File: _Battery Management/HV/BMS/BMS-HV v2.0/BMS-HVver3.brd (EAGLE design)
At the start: 152.4 x 124.8 mm, 423 parts, among them J3 M2S02B-PASK-2(LF)(SN), J4 M2S02B-PASK-2(LF)(SN), Q1 BSS308PE, Q10 BSS308PE, Q11 BSS308PE, Q12 BSS308PE, Q13 BSS308PE, Q14 BSS308PE, Q15 BSS308PE, Q16 BSS308PE, Q17 BSS308PE, Q18 BSS308PE, Q19 BSS308PE, Q2 BSS308PE, Q20 BSS308PE, Q21 BSS308PE, Q22 BSS308PE, Q23 BSS308PE, Q24 BSS308PE, Q25 BSS308PE, Q26 BSS308PE, Q27 BSS308PE, Q28 BSS308PE, Q29 BSS308PE, Q3 BSS308PE, Q30 BSS308PE, Q31 BSS308PE, Q32 BSS308PE, Q33 BSS308PE, Q34 BSS308PE, Q35 BSS308PE, Q36 BSS308PE, Q37 BSS308PE, Q38 BSS308PE, Q39 BSS308PE, Q4 BSS308PE, Q5 BSS308PE, Q6 BSS308PE, Q7 BSS308PE, Q8 BSS308PE, Q9 BSS308PE, U1 LTC6804-2, U2 LTC6804-2, U3 LTC6804-2

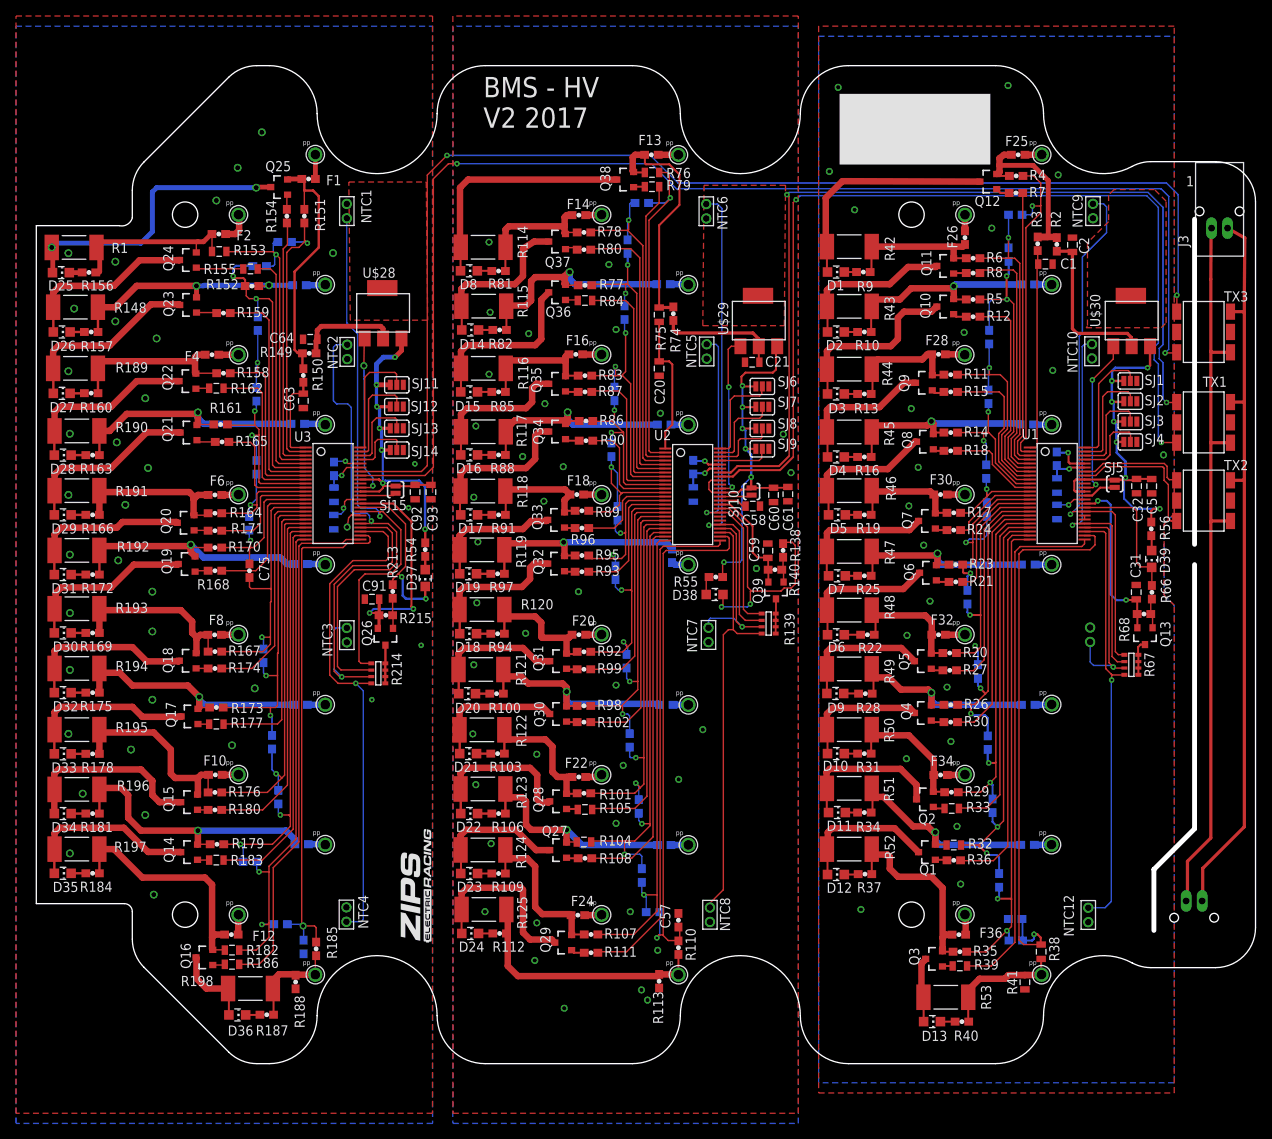
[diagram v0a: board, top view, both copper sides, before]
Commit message: 
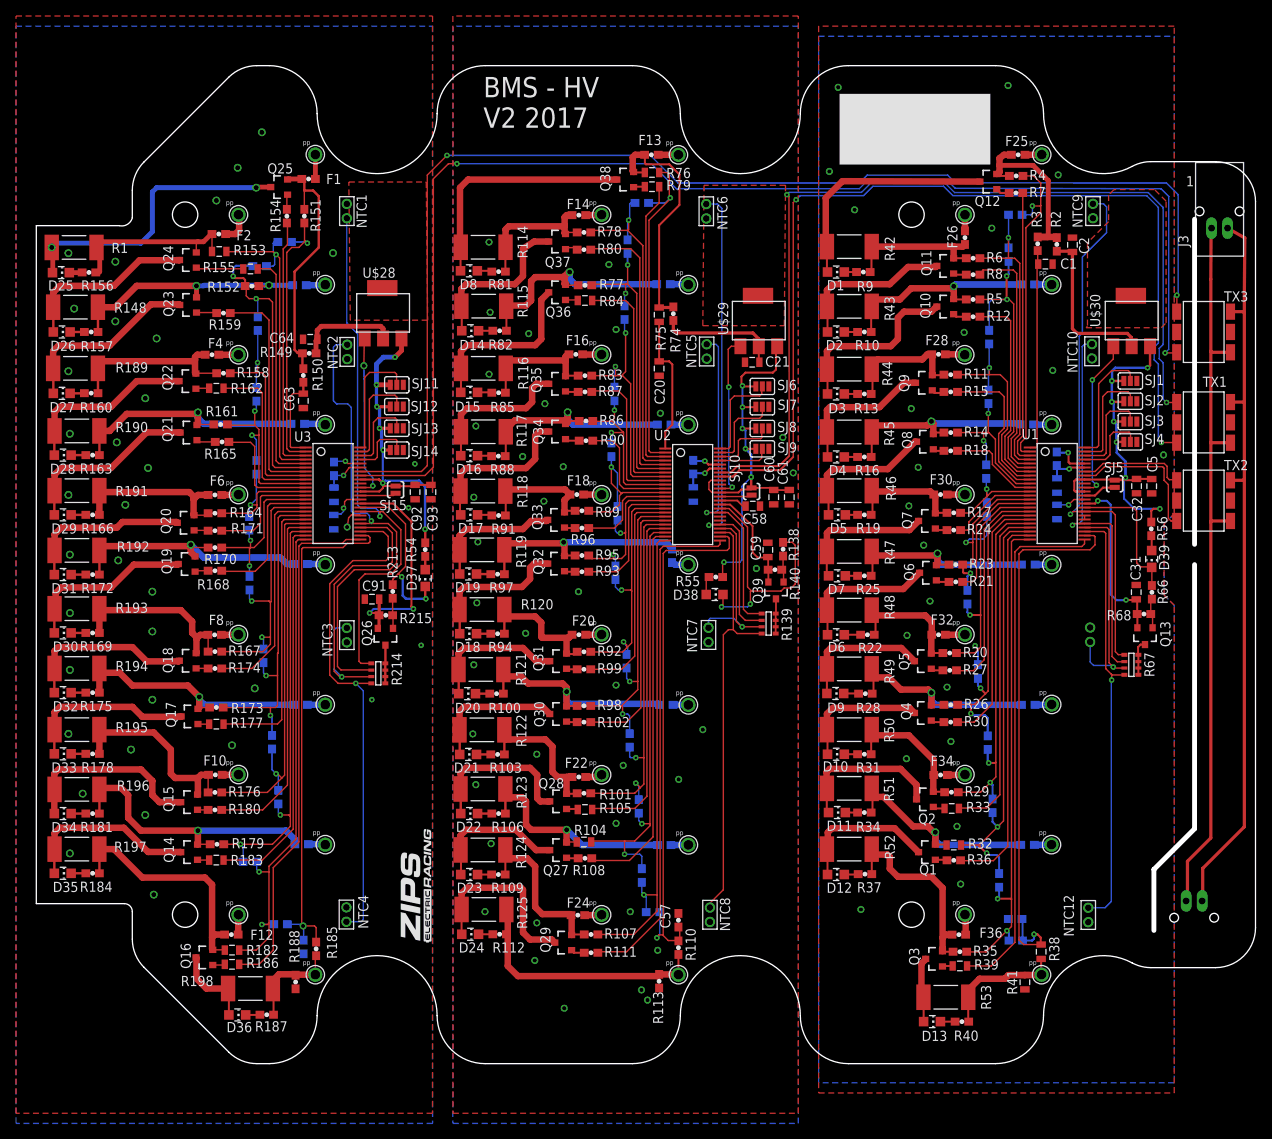
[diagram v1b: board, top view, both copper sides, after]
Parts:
- moved C75 1.55 mm to (-49.6, -2.31), flipped to the bottom
- moved C61 0.42 mm to (17.9, 8.43)
- moved C60 0.28 mm to (16.0, 8.43)
- moved R8 0.20 mm to (40.9, 36.2)
- moved R88 0.15 mm to (-18.4, 13.6)
- moved R138 0.15 mm to (17.1, 1.93)
- moved R109 0.13 mm to (-18.4, -38.7)
- moved D23 0.13 mm to (-22.1, -38.7)
- moved D14 0.10 mm to (-22.0, 29.2)
- moved D21 0.10 mm to (-22.2, -23.7)
- moved R103 0.10 mm to (-18.5, -23.7)
- moved R82 0.10 mm to (-18.3, 29.2)
- moved R85 0.10 mm to (-18.4, 21.5)
- moved C59 0.10 mm to (15.2, 1.84)
- moved D16 0.10 mm to (-22.1, 13.6)
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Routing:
- net C30: track 19.9 -> 21.5 mm, vias 1 -> 2
- net IMA: track 120.5 -> 121.5 mm
- net IPA: track 116.4 -> 117.4 mm
- net IMA2: track 161.4 -> 162.4 mm
- net IPA2: track 156.6 -> 157.4 mm
- net VREG: track 57.8 -> 57.3 mm
- net C31: track 34.3 -> 34.2 mm, vias 1 -> 2

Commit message: 
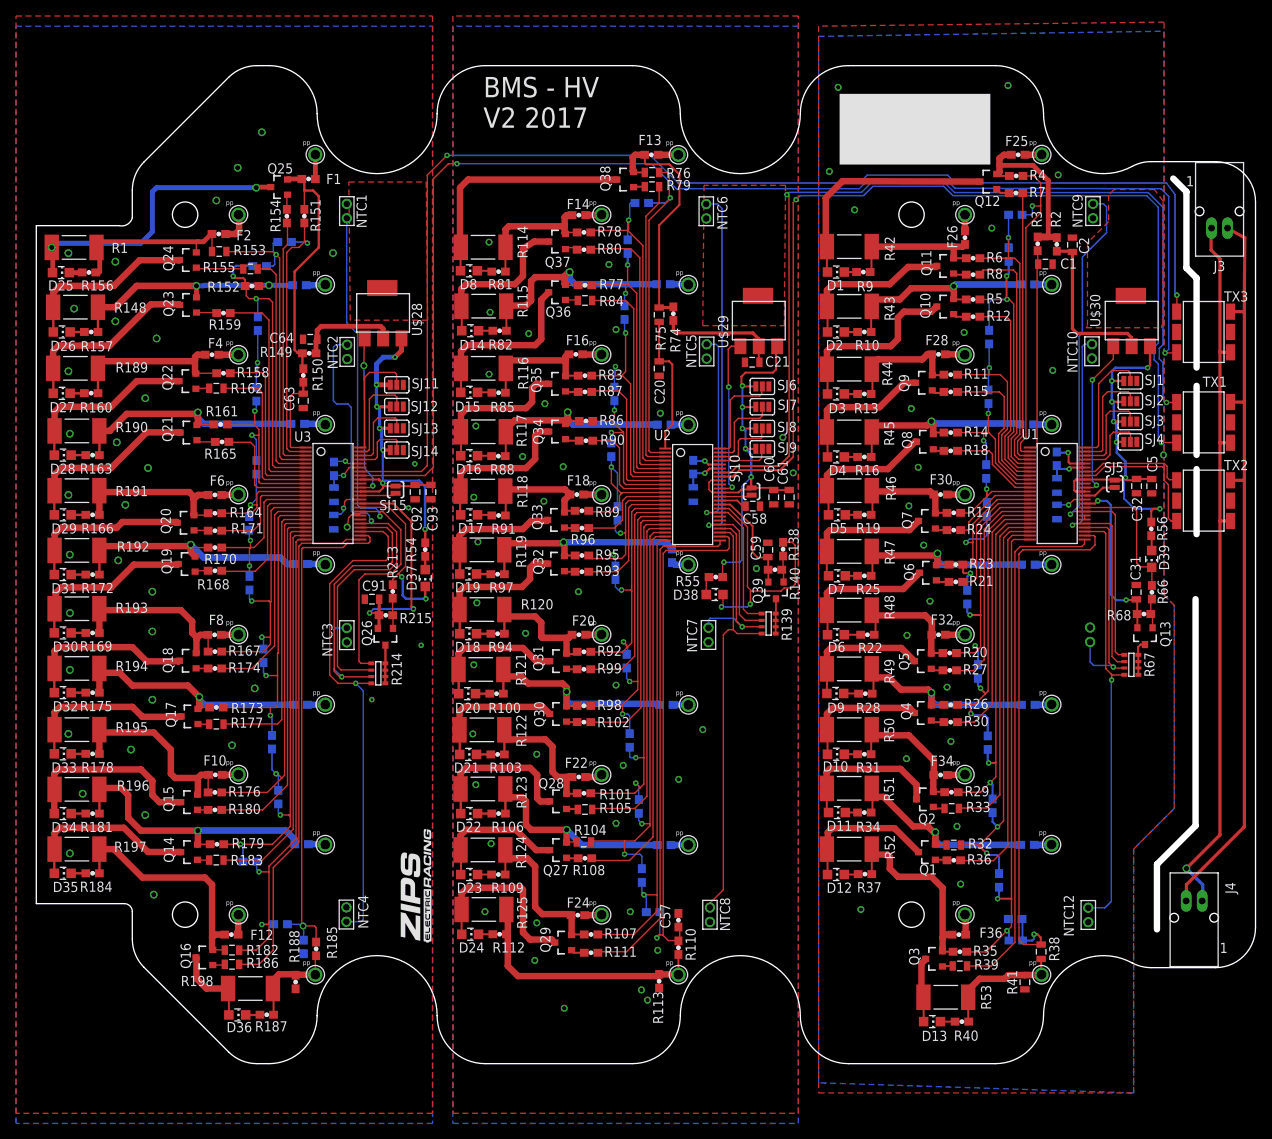
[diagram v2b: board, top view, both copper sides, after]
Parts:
- flipped J4 to the top
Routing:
- net N$129: track 93.2 -> 91.5 mm, vias 0 -> 1
- net N$125: track 92.8 -> 93.7 mm
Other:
- outline, holes or cut-outs redrawn
